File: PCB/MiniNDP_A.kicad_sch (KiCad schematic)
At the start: 21 parts, among them J1 Conn_02x20_Odd_Even, U1 HC161, U2 HC161, U3 HC161, U4 HC138, U5 HC374, U6 AS6C4008, U7 1G32, U8 1G79

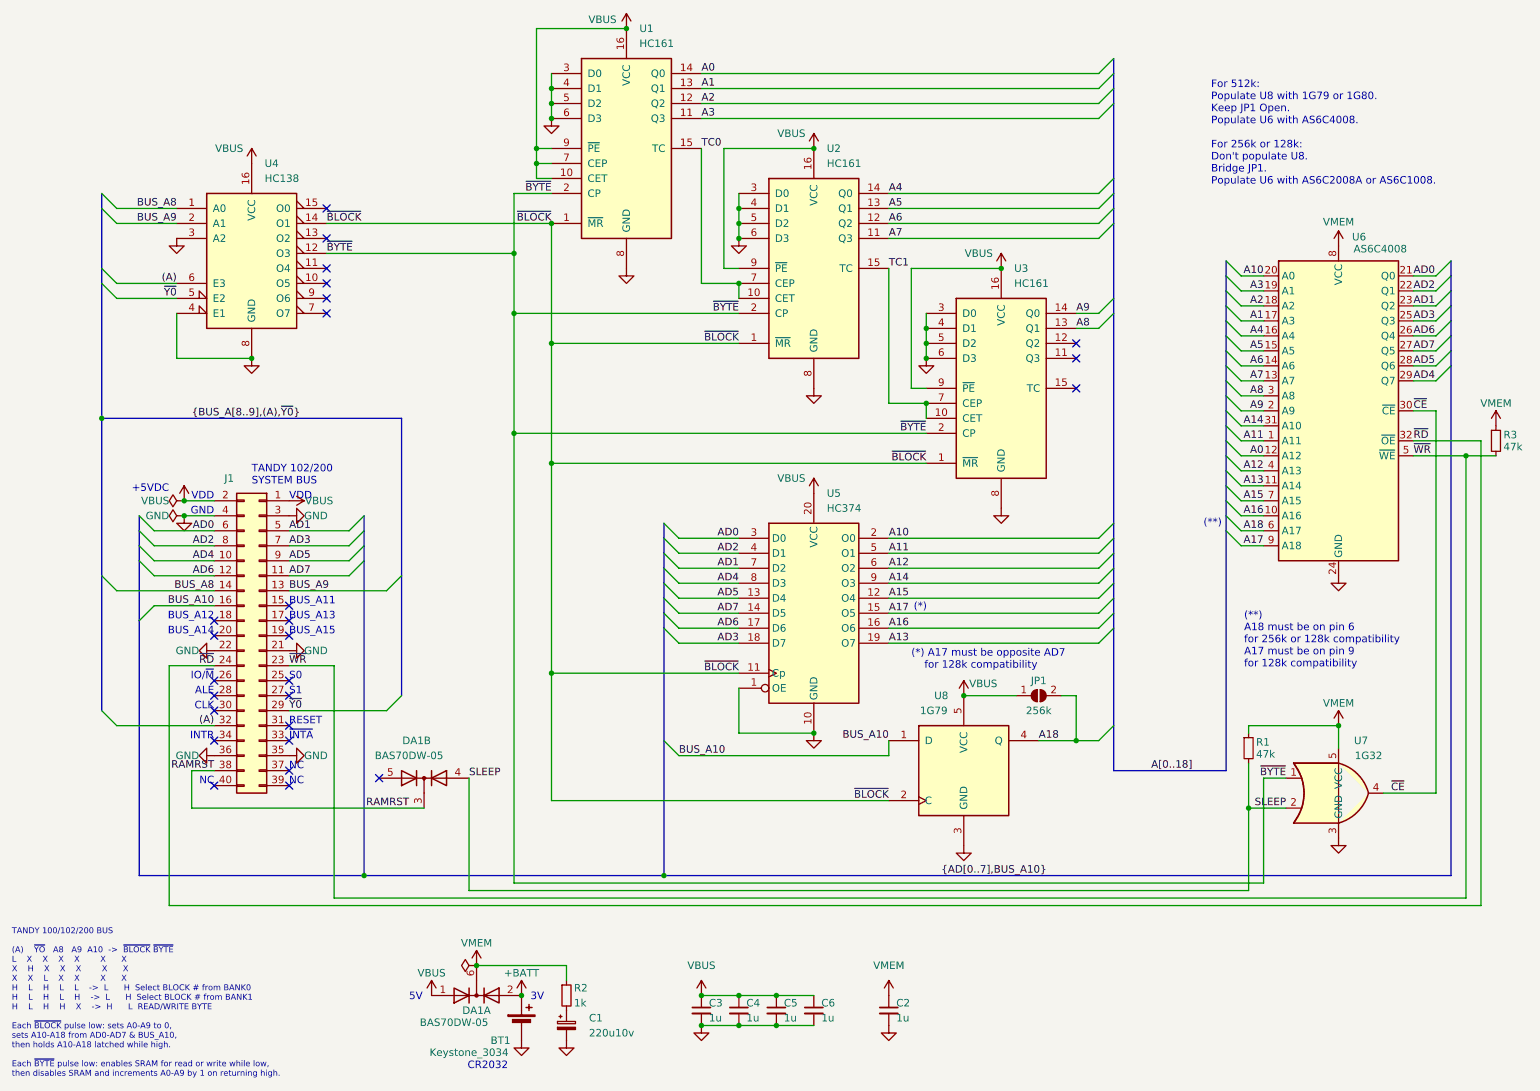
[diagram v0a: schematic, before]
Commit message: make E version default, easier to solder
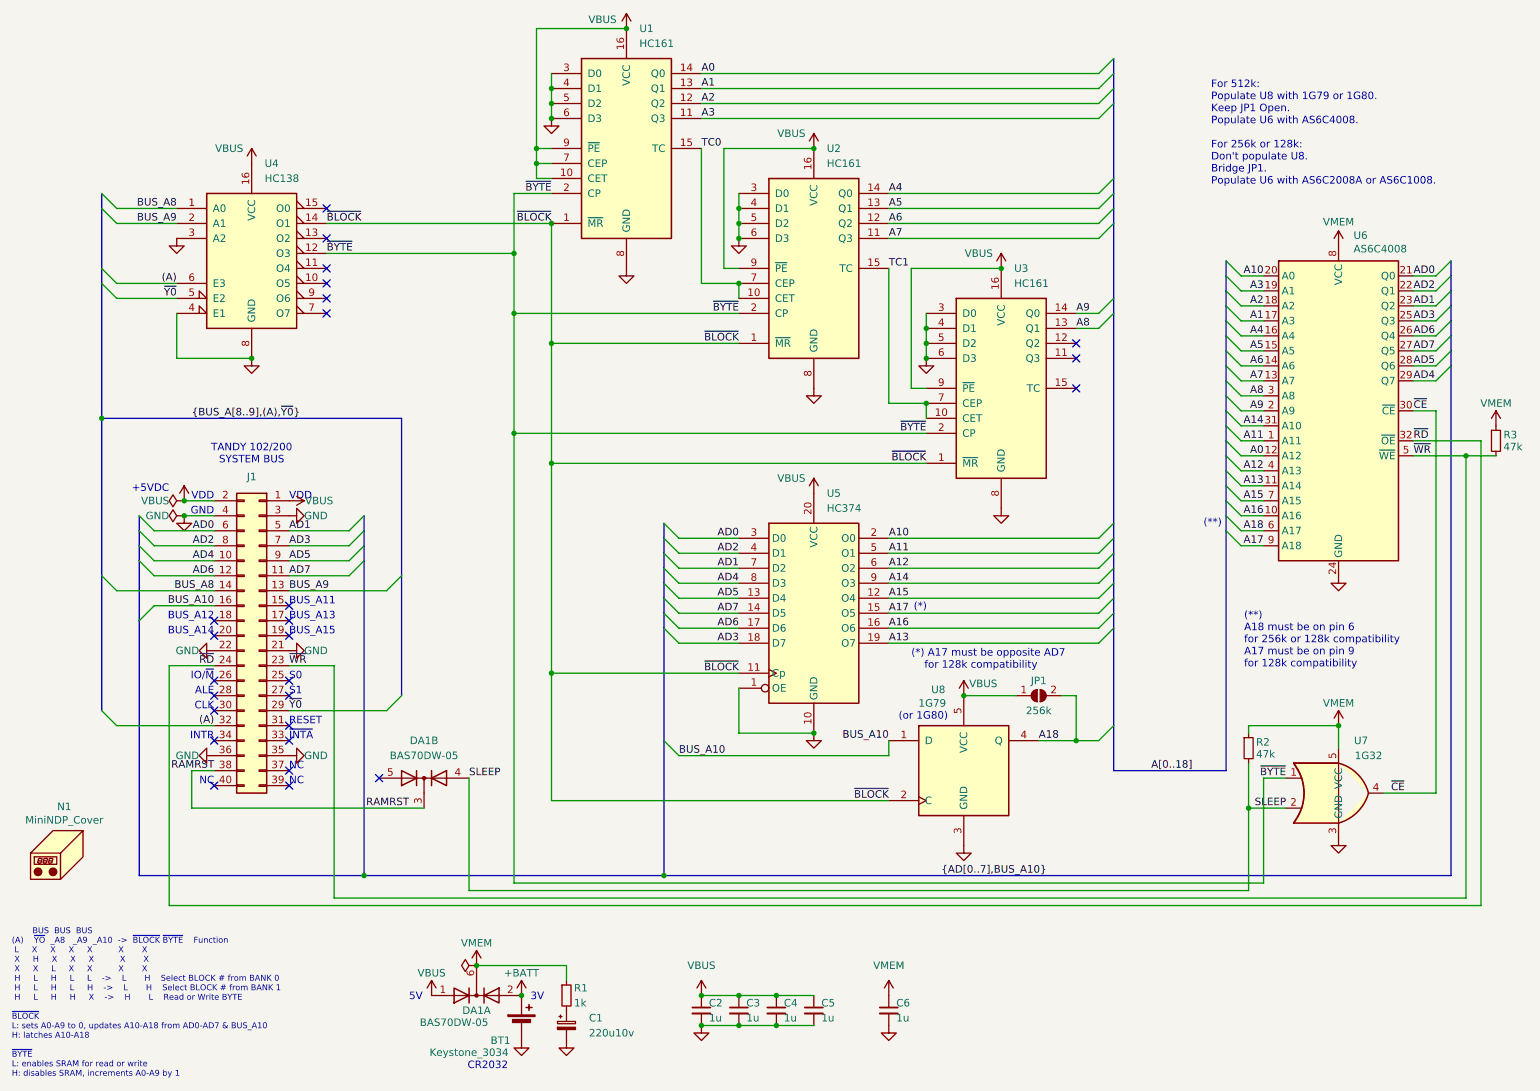
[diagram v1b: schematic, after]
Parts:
- added N1: MiniNDP_Cover, 000_LOCAL:MiniNDP_Cover, symbol 000_LOCAL:Housing
- BT1: MPN (none) -> Keystone 3034
- C1: MPN (none) -> TAJC227K010RNJ
- C2, C3, C4, C5, C6: MPN (none) -> CL21B105KAFNNNE
- DA1: MPN (none) -> BAS70DW-05-7-F
- J1: MPN (none) -> 302-S401
- R1: value 47k -> 1k; MPN (none) -> RK73B2ATTD102J
- R2: value 1k -> 47k; MPN (none) -> RMCF0805FT47K0
- R3: MPN (none) -> RMCF0805FT47K0
- U1, U2, U3: MPN (none) -> 74HC161PW,118
- U4: MPN (none) -> 74HC138PW,118
- U5: MPN (none) -> 74HC374PW,118
- U6: MPN (none) -> AS6C4008-55STIN
- U7: MPN (none) -> 74LVC1G32GW,125
- U8: MPN (none) -> 74LVC1G79GW,125
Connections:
- net SLEEP: now also R2.2; no longer R1.2
- net VBUS: now also C2.1; no longer C6.1
- net VMEM: now also C6.1; no longer C2.1
- net at C1.1: now also R1.2; no longer R2.2
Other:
- note added: "(or 1G80)"
- note added: "BUS BUS BUS (A) ~{YO} _A8 _A9 _A10 -> ~{BLOCK} ~{BYTE} Function L X X X X X X X H X X X X X X X L X X X X H L H L L -> L H Select BLOCK # from BANK 0 H L H L H -> L H Select BLOCK # from BANK 1 H L H H X -> H L Read or Write BYTE ~{BLOCK} L: sets A0-A9 to 0, updates A10-A18 from AD0-AD7 & BUS_A10 H: latches A10-A18 ~{BYTE} L: enables SRAM for read or write H: disables SRAM, increments A0-A9 by 1"
- note removed: "TANDY 100/102/200 BUS (A) ~{YO} A8 A9 A10 -> ~{BLOCK} ~{BYTE} L X X X X X X X H X X X X X X X L X X X X H L H L L -> L H Select BLOCK # from BANK0 H L H L H -> L H Select BLOCK # from BANK1 H L H H X -> H L READ/WRITE BYTE Each ~{BLOCK} pulse low: sets A0-A9 to 0, sets A10-A18 from AD0-AD7 & BUS_A10, then holds A10-A18 latched while high. Each ~{BYTE} pulse low: enables SRAM for read or write whi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"
- title: MiniNDP 512 -> MiniNDP

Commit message: easy boards add 47u cap, remove ramrst diode
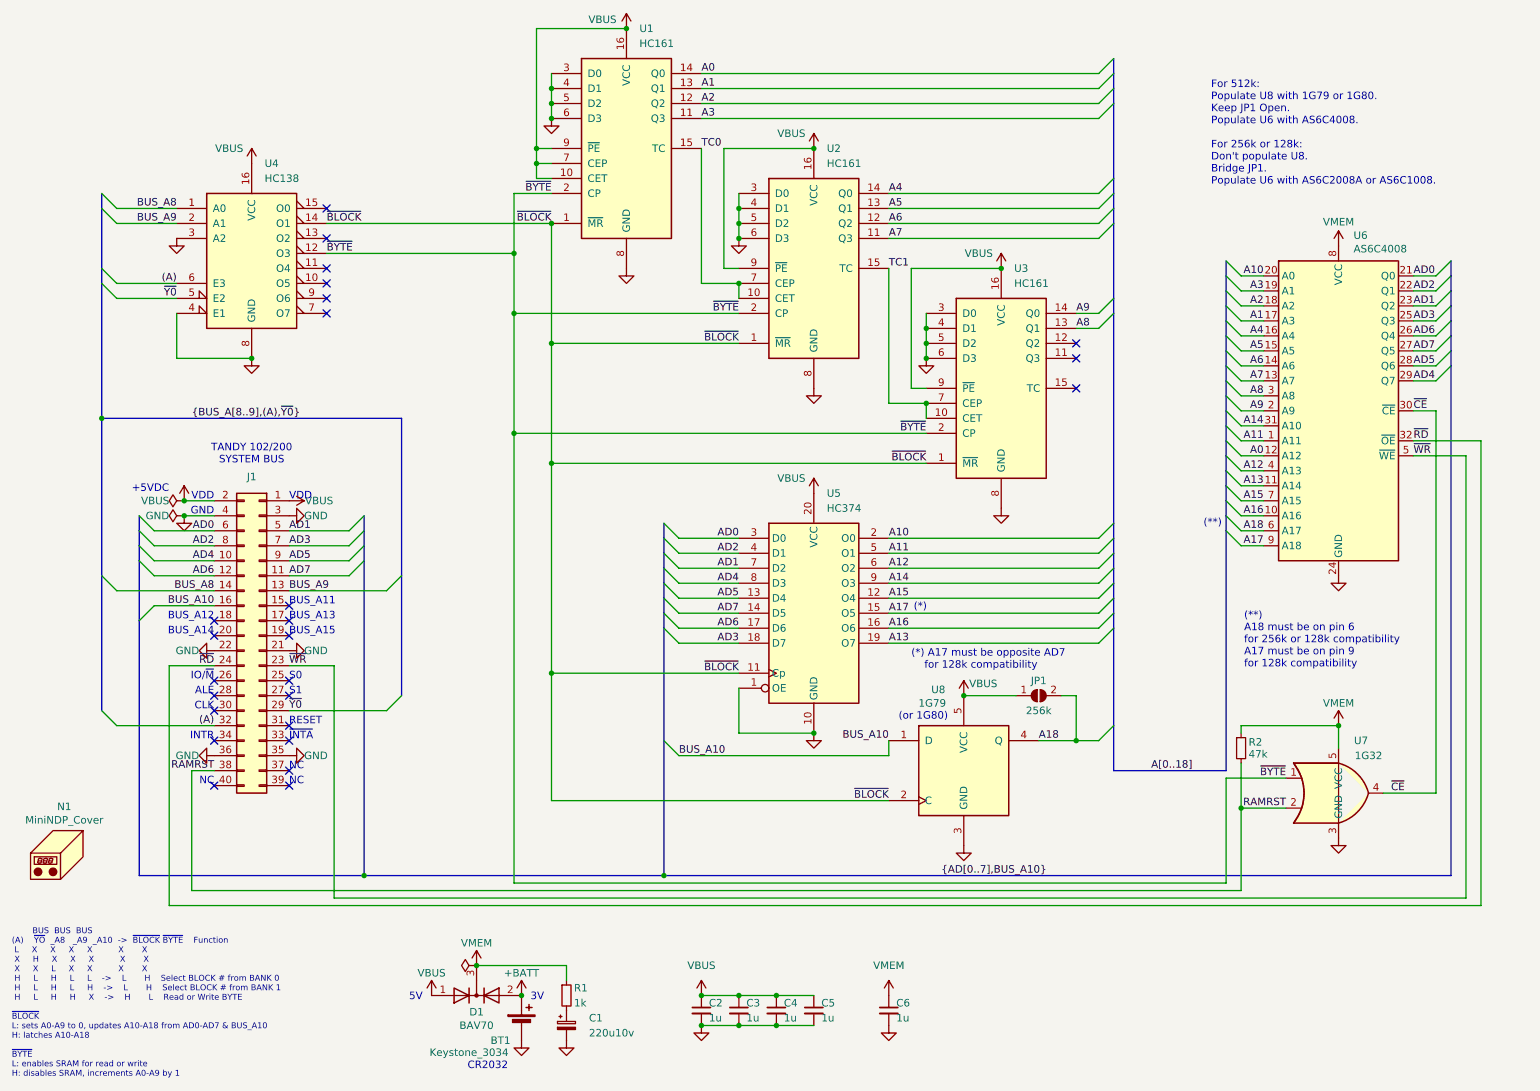
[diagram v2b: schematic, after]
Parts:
- removed DA1: BAS70DW-05, 000_LOCAL:SOT-363_SC-70-6_symmetric, symbol 000_LOCAL:BAV70S
- removed R3: 47k, 000_LOCAL:R_0805, symbol 000_LOCAL:R
- added D1: BAV70, 000_LOCAL:SOT-23, symbol 000_LOCAL:BAV70
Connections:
- net SLEEP is gone; now on net RAMRST: R2.2, U7.2
- net +BATT: now also D1.2 (A)
- net VBUS: now also D1.1 (A)
- net VMEM: now also D1.3 (K)
- no-connect marks 26 -> 25
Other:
- moved on the sheet: R2
